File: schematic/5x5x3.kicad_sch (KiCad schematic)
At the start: 113 parts, among them J1 SW Debug, J2 Battery, SW11 SW, SW12 SW, SW13 SW, SW14 SW, SW15 SW, SW21 SW, SW22 SW, SW23 SW, SW24 SW, SW25 SW, SW31 SW, SW32 SW, SW33 SW, SW34 SW, SW35 SW, SW41 SW, SW42 SW, SW43 SW, SW44 SW, SW45 SW, SW51 SW, SW52 SW, SW53 SW, SW54 SW, SW55 SW, SW6 ALPS_EC11, U1 nice_nano v2

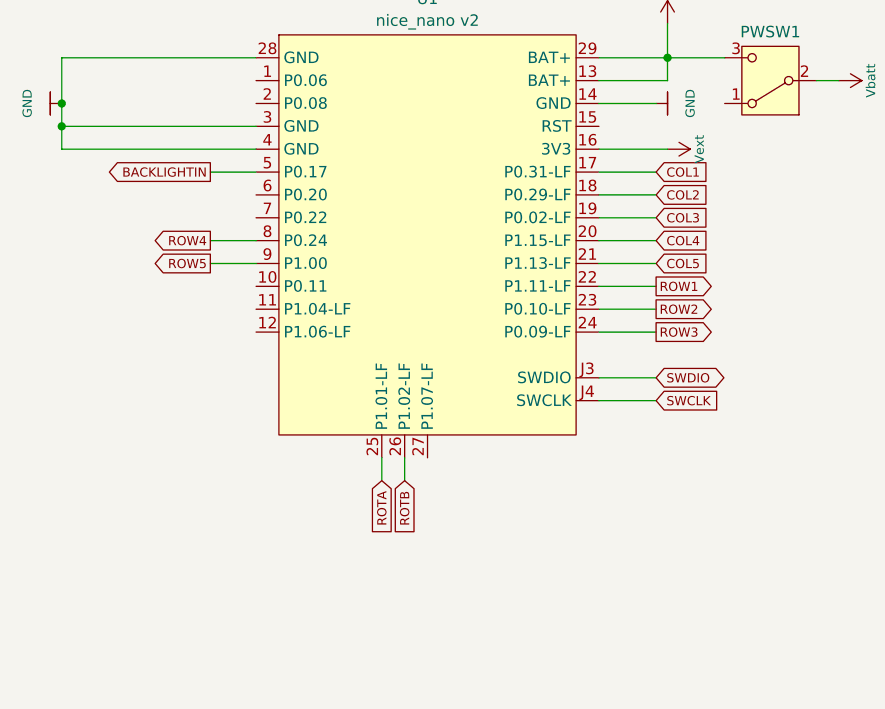
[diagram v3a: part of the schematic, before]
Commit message: Routed rows and columns
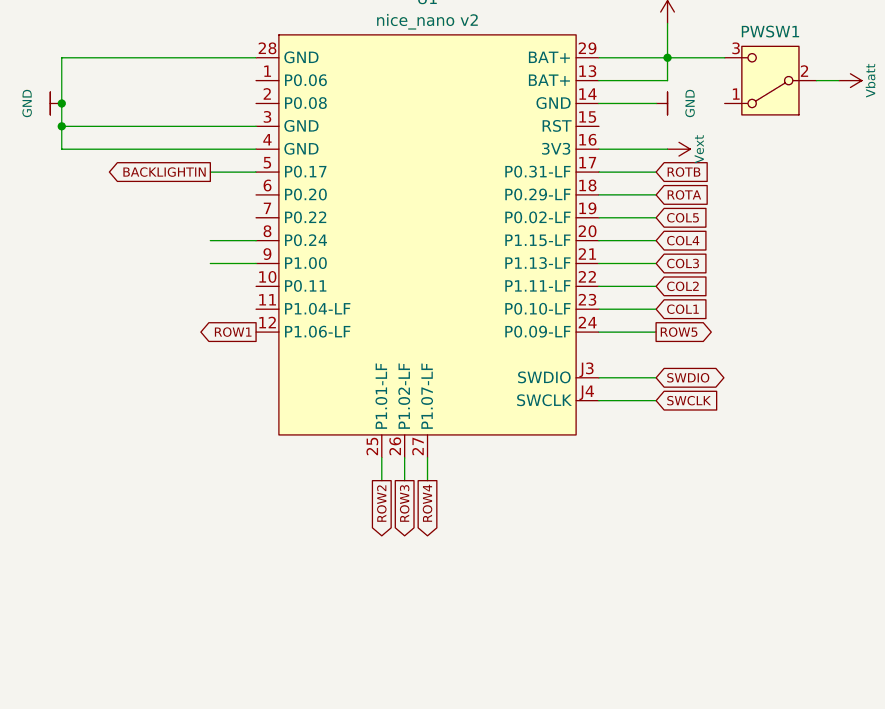
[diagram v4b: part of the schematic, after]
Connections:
- net COL1: now also U1.23 (P0.10-LF); no longer U1.17 (P0.31-LF)
- net COL2: now also U1.22 (P1.11-LF); no longer U1.18 (P0.29-LF)
- net COL3: now also U1.21 (P1.13-LF); no longer U1.19 (P0.02-LF)
- net COL5: now also U1.19 (P0.02-LF); no longer U1.21 (P1.13-LF)
- net ROTA: now also U1.18 (P0.29-LF); no longer U1.25 (P1.01-LF)
- net ROTB: now also U1.17 (P0.31-LF); no longer U1.26 (P1.02-LF)
- net ROTD: now also U1.12 (P1.06-LF); no longer U1.22 (P1.11-LF)
- net ROW2: now also U1.25 (P1.01-LF); no longer U1.23 (P0.10-LF)
- net ROW3: now also U1.26 (P1.02-LF); no longer U1.24 (P0.09-LF)
- net ROW4: now also U1.27 (P1.07-LF); no longer U1.8 (P0.24)
- net ROW5: now also U1.24 (P0.09-LF); no longer U1.9 (P1.00)
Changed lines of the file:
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@@
+	(wire
+		(pts
+			(xy 66.04 91.44) (xy 66.04 93.98)
+		)
+		(stroke
+			(width 0)
+			(type default)
+		)
+	)
 	(wire
 		(pts
@@
 	(global_label "COL3"
 		(shape input)
-		(at 91.44 64.77 0)
+		(at 91.44 69.85 0)
 		(fields_autoplaced yes)
 		(effects
@@
 		)
 		(property "Intersheetrefs" "${INTERSHEET_REFS}"
-			(at 97.6984 64.77 0)
+			(at 97.6984 69.85 0)
 			(effects
 				(font
@@
 	(global_label "COL2"
 		(shape input)
-		(at 91.44 62.23 0)
+		(at 91.44 72.39 0)
 		(fields_autoplaced yes)
 		(effects
@@
 		)
 		(property "Intersheetrefs" "${INTERSHEET_REFS}"
-			(at 97.6984 62.23 0)
+			(at 97.6984 72.39 0)
 			(effects
 				(font
@@
 	(global_label "ROTA"
 		(shape input)
-		(at 60.96 93.98 270)
-		(fields_autoplaced yes)
-		(effects
-			(font
-				(size 1.016 1.016)
-			)
-			(justify right)
-		)
-		(property "Intersheetrefs" "${INTERSHEET_REFS}"
-			(at 60.96 100.0933 90)
+		(at 91.44 62.23 0)
+		(fields_autoplaced yes)
+		(effects
+			(font
+				(size 1.016 1.016)
+			)
+			(justify left)
+		)
+		(property "Intersheetrefs" "${INTERSHEET_REFS}"
+			(at 97.5533 62.23 0)
 			(effects
 				(font
 					(size 1.016 1.016)
 				)
-				(justify right)
+				(justify left)
 				(hide yes)
 			)
@@
 	(global_label "COL1"
 		(shape input)
-		(at 91.44 59.69 0)
+		(at 91.44 74.93 0)
 		(fields_autoplaced yes)
 		(effects
@@
 		)
 		(property "Intersheetrefs" "${INTERSHEET_REFS}"
-			(at 97.6984 59.69 0)
+			(at 97.6984 74.93 0)
 			(effects
 				(font
@@
 	(global_label "ROTB"
 		(shape input)
-		(at 63.5 93.98 270)
-		(fields_autoplaced yes)
-		(effects
-			(font
-				(size 1.016 1.016)
-			)
-			(justify right)
-		)
-		(property "Intersheetrefs" "${INTERSHEET_REFS}"
-			(at 63.5 100.2384 90)
+		(at 91.44 59.69 0)
+		(fields_autoplaced yes)
+		(effects
+			(font
+				(size 1.016 1.016)
+			)
+			(justify left)
+		)
+		(property "Intersheetrefs" "${INTERSHEET_REFS}"
+			(at 97.6984 59.69 0)
 			(effects
 				(font
 					(size 1.016 1.016)
 				)
-				(justify right)
+				(justify left)
 				(hide yes)
 			)
@@
 	(global_label "ROW5"
 		(shape output)
-		(at 41.91 69.85 180)
-		(fields_autoplaced yes)
-		(effects
-			(font
-				(size 1.016 1.016)
-			)
-			(justify right)
-		)
-		(property "Intersheetrefs" "${INTERSHEET_REFS}"
-			(at -49.53 -17.78 0)
-			(effects
-				(font
-					(size 1.27 1.27)
-				)
+		(at 91.44 77.47 0)
+		(fields_autoplaced yes)
+		(effects
+			(font
+				(size 1.016 1.016)
+			)
+			(justify left)
+		)
+		(property "Intersheetrefs" "${INTERSHEET_REFS}"
+			(at 98.037 77.47 0)
+			(effects
+				(font
+					(size 1.27 1.27)
+				)
+				(justify left)
 				(hide yes)
 			)
@@
 	(global_label "ROW2"
 		(shape output)
-		(at 91.44 74.93 0)
-		(fields_autoplaced yes)
-		(effects
-			(font
-				(size 1.016 1.016)
-			)
-			(justify left)
-		)
-		(property "Intersheetrefs" "${INTERSHEET_REFS}"
-			(at 98.037 74.93 0)
-			(effects
-				(font
-					(size 1.27 1.27)
-				)
-				(justify left)
+		(at 60.96 93.98 270)
+		(fields_autoplaced yes)
+		(effects
+			(font
+				(size 1.016 1.016)
+			)
+			(justify right)
+		)
+		(property "Intersheetrefs" "${INTERSHEET_REFS}"
+			(at 60.96 100.577 90)
+			(effects
+				(font
+					(size 1.27 1.27)
+				)
+				(justify right)
 				(hide yes)
 			)
@@
 	(global_label "COL5"
 		(shape input)
-		(at 91.44 69.85 0)
+		(at 91.44 64.77 0)
 		(fields_autoplaced yes)
 		(effects
@@
 		)
 		(property "Intersheetrefs" "${INTERSHEET_REFS}"
-			(at -99.06 20.32 0)
+			(at -99.06 15.24 0)
 			(effects
 				(font
@@
 	(global_label "ROW4"
 		(shape output)
-		(at 41.91 67.31 180)
+		(at 66.04 93.98 270)
 		(fields_autoplaced yes)
 		(effects
@@
 		)
 		(property "Intersheetrefs" "${INTERSHEET_REFS}"
-			(at -49.53 -17.78 0)
-			(effects
-				(font
-					(size 1.27 1.27)
-				)
+			(at 66.04 100.577 90)
+			(effects
+				(font
+					(size 1.27 1.27)
+				)
+				(justify right)
 				(hide yes)
 			)
@@
 	(global_label "ROW1"
 		(shape output)
-		(at 91.44 72.39 0)
-		(fields_autoplaced yes)
-		(effects
-			(font
-				(size 1.016 1.016)
-			)
-			(justify left)
-		)
-		(property "Intersheetrefs" "${INTERSHEET_REFS}"
-			(at 98.037 72.39 0)
-			(effects
-				(font
-					(size 1.27 1.27)
-				)
-				(justify left)
+		(at 46.99 77.47 180)
+		(fields_autoplaced yes)
+		(effects
+			(font
+				(size 1.016 1.016)
+			)
+			(justify right)
+		)
+		(property "Intersheetrefs" "${INTERSHEET_REFS}"
+			(at 40.393 77.47 0)
+			(effects
+				(font
+					(size 1.27 1.27)
+				)
+				(justify right)
 				(hide yes)
 			)
@@
 	(global_label "ROW3"
 		(shape output)
-		(at 91.44 77.47 0)
-		(fields_autoplaced yes)
-		(effects
-			(font
-				(size 1.016 1.016)
-			)
-			(justify left)
-		)
-		(property "Intersheetrefs" "${INTERSHEET_REFS}"
-			(at 98.037 77.47 0)
-			(effects
-				(font
-					(size 1.27 1.27)
-				)
-				(justify left)
-				(hide yes)
-			)
+		(at 63.5 93.98 270)
+		(fields_autoplaced yes)
+		(effects
+			(font
+				(size 1.016 1.016)
+			)
+			(justify right)
+		)
+		(property "Intersheetrefs" "${INTERSHEET_REFS}"
+			(at 63.5 100.577 90)
+			(effects
+				(font
+					(size 1.27 1.27)
+				)
+				(justify right)
+				(hide yes)
+			)

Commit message: Leds now connected to right pin 0.22
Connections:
- net BACKLIGHTIN: now also U1.7 (P0.22); no longer U1.5 (P0.17)
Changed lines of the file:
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@@
 	(wire
 		(pts
+			(xy 40.64 77.47) (xy 46.99 77.47)
+		)
+		(stroke
+			(width 0)
+			(type default)
+		)
+	)
+	(wire
+		(pts
 			(xy 210.82 234.95) (xy 208.28 234.95)
 		)
@@
 	(wire
 		(pts
-			(xy 41.91 59.69) (xy 46.99 59.69)
-		)
-		(stroke
-			(width 0)
-			(type default)
-		)
-	)
-	(wire
-		(pts
 			(xy 172.72 260.35) (xy 170.18 260.35)
 		)
@@
 	(wire
 		(pts
+			(xy 40.64 64.77) (xy 46.99 64.77)
+		)
+		(stroke
+			(width 0)
+			(type default)
+		)
+	)
+	(wire
+		(pts
 			(xy 49.53 135.89) (xy 49.53 142.24)
 		)
@@
 	(global_label "BACKLIGHTIN"
 		(shape output)
-		(at 41.91 59.69 180)
+		(at 40.64 64.77 180)
 		(fields_autoplaced yes)
 		(effects
@@
 		)
 		(property "Intersheetrefs" "${INTERSHEET_REFS}"
-			(at 30.3518 59.6265 0)
+			(at 29.0818 64.7065 0)
 			(effects
 				(font
@@
 	(global_label "ROW1"
 		(shape output)
-		(at 46.99 77.47 180)
+		(at 40.64 77.47 180)
 		(fields_autoplaced yes)
 		(effects
@@
 		)
 		(property "Intersheetrefs" "${INTERSHEET_REFS}"
-			(at 40.393 77.47 0)
+			(at 34.043 77.47 0)
 			(effects
 				(font

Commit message: Routed cols and rows
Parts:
- added J10, J13, J14, J16, J5, J6, J9: Conn_01x03_Female, Connector_PinSocket_2.54mm:PinSocket_1x03_P2.54mm_Vertical, symbol Connector:Conn_01x03_Female
- added J11, J12, J15, J3, J4, J7, J8: Conn_01x03_Male, Connector_PinSocket_2.54mm:PinSocket_1x03_P2.54mm_Vertical, symbol Connector:Conn_01x03_Male
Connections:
- net BACKLIGHTIN: now also J10.1 (Pin_1), J8.1 (Pin_1)
- net COL1: now also J12.1 (Pin_1), J14.1 (Pin_1)
- net COL2: now also J12.2 (Pin_2), J14.2 (Pin_2)
- net COL3: now also J12.3 (Pin_3), J14.3 (Pin_3)
- net COL4: now also J11.1 (Pin_1), J13.1 (Pin_1)
- net COL5: now also J11.2 (Pin_2), J13.2 (Pin_2)
- net GND: now also J3.1 (Pin_1), J3.2 (Pin_2), J4.1 (Pin_1), J5.1 (Pin_1), J5.2 (Pin_2), J6.1 (Pin_1)
- net ROTA: now also J15.2 (Pin_2), J16.2 (Pin_2)
- net ROTB: now also J15.3 (Pin_3), J16.3 (Pin_3)
- net ROTD: now also J10.2 (Pin_2), J8.2 (Pin_2)
- net ROW2: now also J10.3 (Pin_3), J8.3 (Pin_3)
- net ROW3: now also J7.1 (Pin_1), J9.1 (Pin_1)
- net ROW4: now also J7.2 (Pin_2), J9.2 (Pin_2)
- net ROW5: now also J7.3 (Pin_3), J9.3 (Pin_3)
- net Vext: now also J4.2 (Pin_2), J4.3 (Pin_3), J6.2 (Pin_2), J6.3 (Pin_3)
- net Vpowered: now also J3.3 (Pin_3), J5.3 (Pin_3)
- net BACKLIGHTOUT: now reaches LED55.2 (DOUT), R20.1
- net BACKLIGHTOUT: now also J11.3 (Pin_3), J13.3 (Pin_3)

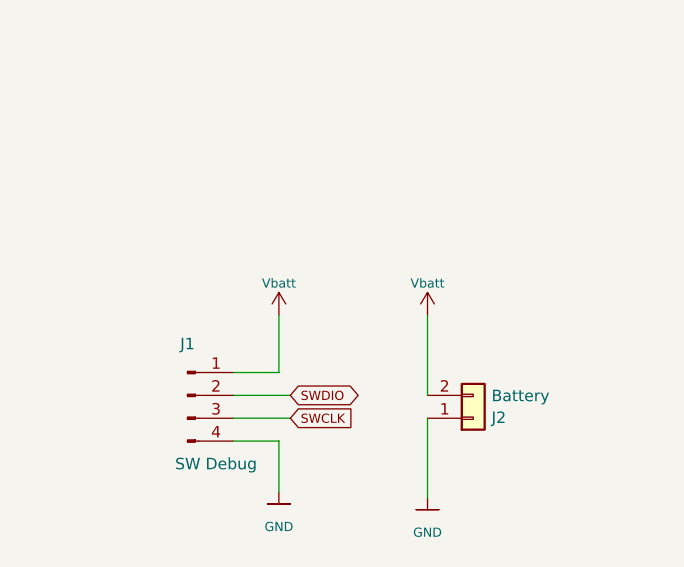
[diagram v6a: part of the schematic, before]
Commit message: Adjusted layer indications, component label legibility, routed mcu
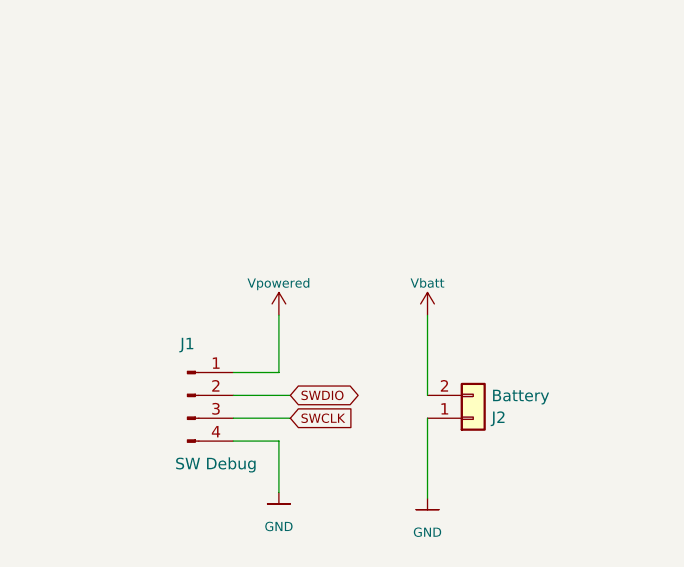
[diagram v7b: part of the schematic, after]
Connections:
- net Vbatt: no longer J1.1 (Pin_1)
- net Vpowered: now also J1.1 (Pin_1)
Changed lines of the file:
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@@
 	)
 	(symbol
+		(lib_id "usb:Vusb")
+		(at 49.53 135.89 0)
+		(unit 1)
+		(exclude_from_sim no)
+		(in_bom yes)
+		(on_board yes)
+		(dnp no)
+		(property "Reference" "#PWR01"
+			(at 49.53 139.7 0)
+			(effects
+				(font
+					(size 1.27 1.27)
+				)
+				(hide yes)
+			)
+		)
+		(property "Value" "Vpowered"
+			(at 49.53 132.334 0)
+			(effects
+				(font
+					(size 1.016 1.016)
+				)
+			)
+		)
+		(property "Footprint" ""
+			(at 49.53 135.89 0)
+			(effects
+				(font
+					(size 1.524 1.524)
+				)
+			)
+		)
+		(property "Datasheet" ""
+			(at 49.53 139.7 0)
+			(effects
+				(font
+					(size 1.524 1.524)
+				)
+			)
+		)
+		(property "Description" ""
+			(at 49.53 135.89 0)
+			(effects
+				(font
+					(size 1.27 1.27)
+				)
+				(hide yes)
+			)
+		)
+		(pin "1"
+		)
+		(instances
+			(project "5x5x3"
+				(path "/e63e39d7-6ac0-4ffd-8aa3-1841a4541b55"
+					(reference "#PWR01")
+					(unit 1)
+				)
+			)
+		)
+	)
+	(symbol
 		(lib_id "SK68xx:SK6812MINI-E")
 		(at 295.91 38.1 0)
@@
 					(unit 1)
 				)
-			)
-		)
-	)
-	(symbol
-		(lib_id "power:+3V3")
-		(at 49.53 135.89 0)
-		(unit 1)
-		(exclude_from_sim no)
-		(in_bom yes)
-		(on_board yes)
-		(dnp no)
-		(property "Reference" "#PWR01"
-			(at 49.53 139.7 0)
-			(effects
-				(font
-					(size 1.27 1.27)
-				)
-				(hide yes)
-			)
-		)
-		(property "Value" "Vbatt"
-			(at 49.53 132.334 0)
-			(effects
-				(font
-					(size 1.016 1.016)
-				)
-			)
-		)
-		(property "Footprint" ""
-			(at 49.53 135.89 0)
-			(effects
-				(font
-					(size 1.27 1.27)
-				)
-				(hide yes)
-			)
-		)
-		(property "Datasheet" ""
-			(at 49.53 135.89 0)
-			(effects
-				(font
-					(size 1.27 1.27)
-				)
-				(hide yes)
-			)
-		)
-		(property "Description" ""
-			(at 49.53 135.89 0)
-			(effects
-				(font
-					(size 1.27 1.27)
-				)
-				(hide yes)
-			)
-		)
-		(pin "1"
-		)
-		(instances
-			(project "5x5x2"
-				(path "/e63e39d7-6ac0-4ffd-8aa3-1841a4541b55"
-					(reference "#PWR01")
-					(unit 1)
-				)
